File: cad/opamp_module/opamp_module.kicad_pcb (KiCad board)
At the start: 2 copper layers, 46.5 x 35.5 mm, 28 parts, among them J1 Conn_02x04_Odd_Even, U1 OPA2325, U2 REF3433IDBVR

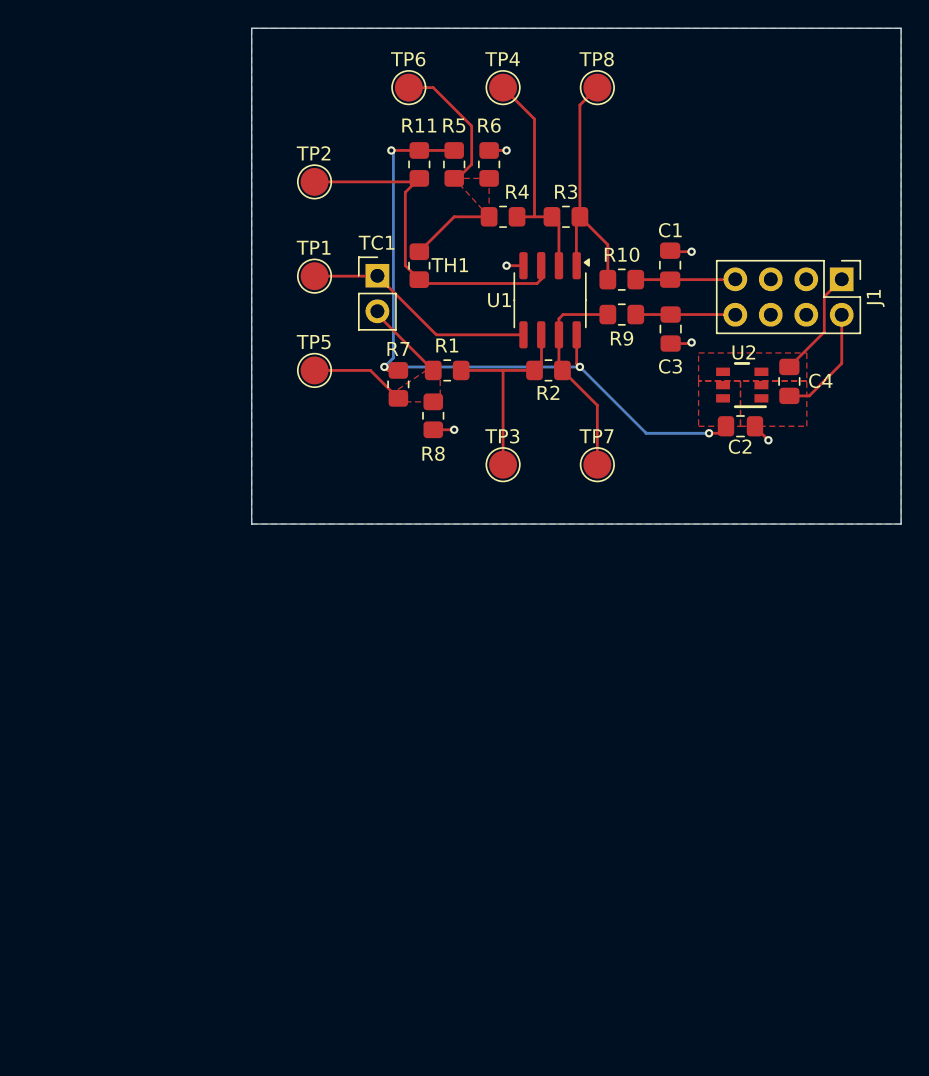
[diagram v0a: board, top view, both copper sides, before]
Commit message: Spice simulations and switching to two TC's per module
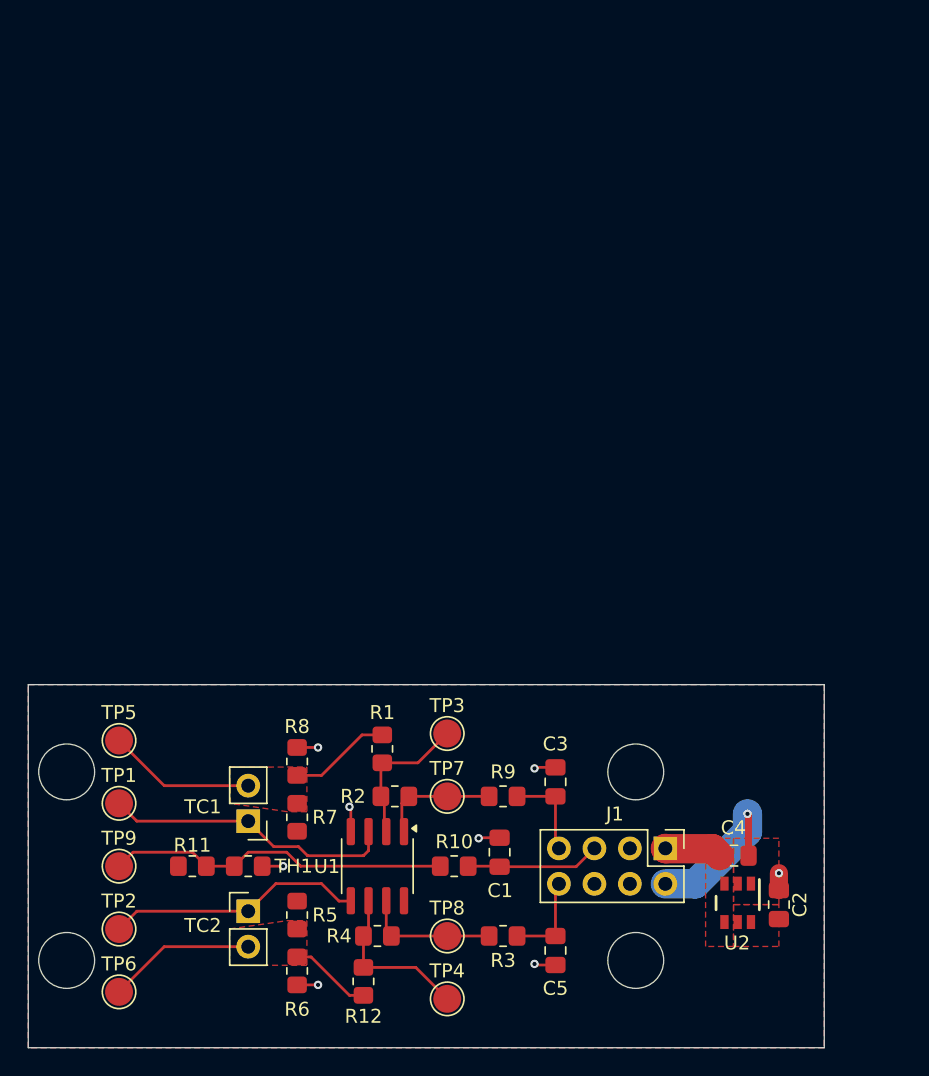
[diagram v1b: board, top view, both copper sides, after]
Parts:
- added C5: 47n, Capacitor_SMD:C_0805_2012Metric_Pad1.18x1.45mm_HandSolder, F.Cu at (143.8, 140.0)
- added R12: 10k, Resistor_SMD:R_0805_2012Metric_Pad1.20x1.40mm_HandSolder, F.Cu at (130.0, 142.2)
- added TC2: Thermocouple, Connector_PinHeader_2.54mm:PinHeader_1x02_P2.54mm_Vertical, F.Cu at (121.8, 137.2)
- added TP9: TestPoint, TestPoint:TestPoint_Pad_D2.0mm, F.Cu at (112.5, 134.0)
- R1: value 1M -> 10k
- R10, R9: value 1.7k -> 3386
- R11: value 3M3 -> 10k
- R2: value 32M -> 340k
- R3: value 12M -> 3386
- R4: value 1M -> 340k
- R5, R7: value 9000 -> 90k
- R6: value 2000 -> 500
- R8: value 4000 -> 500
- moved TP6 68.0 mm to (112.5, 143.0)
- moved TP4 65.4 mm to (136.0, 143.5)
- moved TP8 61.7 mm to (136.0, 139.0)
- moved R6 59.4 mm to (125.2, 141.5), turned to -90 degrees
- moved TP2 55.3 mm to (112.5, 138.5)
- moved R5 54.9 mm to (125.2, 137.5)
- moved R11 52.8 mm to (117.8, 134.0), turned to 180 degrees
- moved R4 52.3 mm to (131.0, 139.0)
- moved R3 51.7 mm to (140.0, 139.0), turned to 0 degrees
- moved TH1 44.7 mm to (121.8, 134.0), turned to 180 degrees
- moved C1 43.8 mm to (139.8, 133.0)
- moved R10 43.7 mm to (136.5, 134.0)
- moved J1 42.7 mm to (151.6, 132.7)
- moved U1 42.4 mm to (131.0, 134.0)
- moved TP1 40.3 mm to (112.5, 129.5)
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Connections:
- C3 pad 1: ThemoCoupleFiltered -> ThermoCoupleFiltered_{0}
- J1 pad 5: unconnected-(J1-Pin_5-Pad5) -> ThermistorFiltered
- J1 pad 7: ThermistorFiltered -> ThermoCoupleFiltered_{0}
- J1 pad 8: ThemoCoupleFiltered -> ThermoCoupleFiltered_{1}
- R1 pad 1: Net-(U1B--) -> OffsetReferenceThermoCouple_{0}
- R1 pad 2: OffsetReferenceThermoCouple -> Net-(U1A--)
- R11 pad 1: Net-(U1A-+) -> ThermistorUnfiltered
- R2 pad 1: ThemoCoupleUnfiltered -> ThermoCoupleUnfiltered_{0}
- R2 pad 2: Net-(U1B--) -> Net-(U1A--)
- R3 pad 1: ThermistorUnfiltered -> ThermoCoupleUnfiltered_{1}
- R3 pad 2: Net-(U1A--) -> ThermoCoupleFiltered_{1}
- R4 pad 1: Net-(U1A--) -> ThermoCoupleUnfiltered_{1}
- R4 pad 2: OffsetReferenceThermistor -> Net-(U1B--)
- R5 pad 2: OffsetReferenceThermistor -> OffsetReferenceThermoCouple_{1}
- R6 pad 1: OffsetReferenceThermistor -> OffsetReferenceThermoCouple_{1}
- R7 pad 2: OffsetReferenceThermoCouple -> OffsetReferenceThermoCouple_{0}
- R8 pad 1: OffsetReferenceThermoCouple -> OffsetReferenceThermoCouple_{0}
- R9 pad 1: ThemoCoupleUnfiltered -> ThermoCoupleUnfiltered_{0}
- R9 pad 2: ThemoCoupleFiltered -> ThermoCoupleFiltered_{0}
- TC1 pad 2: OffsetReferenceThermoCouple -> OffsetReferenceThermoCouple_{0}
- TH1 pad 1: OffsetReferenceThermistor -> GND
- TH1 pad 2: Net-(U1A-+) -> ThermistorUnfiltered
- TP2 pad 1: Net-(U1A-+) -> Net-(TC2-+)
- TP3 pad 1: Net-(U1B--) -> Net-(U1A--)
- TP4 pad 1: Net-(U1A--) -> Net-(U1B--)
- TP5 pad 1: OffsetReferenceThermoCouple -> OffsetReferenceThermoCouple_{0}
- TP6 pad 1: OffsetReferenceThermistor -> OffsetReferenceThermoCouple_{1}
- TP7 pad 1: ThemoCoupleUnfiltered -> ThermoCoupleUnfiltered_{0}
- TP8 pad 1: ThermistorUnfiltered -> ThermoCoupleUnfiltered_{1}
- U1 pad 1: ThermistorUnfiltered -> ThermoCoupleUnfiltered_{0}
- U1 pad 3: Net-(U1A-+) -> Net-(TC1-+)
- U1 pad 5: Net-(TC1-+) -> Net-(TC2-+)
- U1 pad 7: ThemoCoupleUnfiltered -> ThermoCoupleUnfiltered_{1}
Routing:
- net +3.3VA: track 50.5 -> 0.00 mm, vias 4 -> 0
- net Net-(U1A-+): track 25.6 -> 0.00 mm
- net Net-(TC2-+): track 0.00 -> 18.5 mm
- net OffsetReferenceThermoCouple_{0}: track 0.00 -> 17.9 mm
- net OffsetReferenceThermoCouple_{1}: track 0.00 -> 16.5 mm
- net OffsetReferenceThermistor: track 15.8 -> 0.00 mm
- net ThemoCoupleUnfiltered: track 15.2 -> 0.00 mm
- net OffsetReferenceThermoCouple: track 12.7 -> 0.00 mm
- net ThermoCoupleUnfiltered_{1}: track 0.00 -> 9.68 mm
- net ThermoCoupleUnfiltered_{0}: track 0.00 -> 8.55 mm
- net GND: track 16.7 -> 23.8 mm, vias 6 -> 9
- net ThemoCoupleFiltered: track 7.14 -> 0.00 mm
- net ThermoCoupleFiltered_{0}: track 0.00 -> 7.06 mm
- net ThermoCoupleFiltered_{1}: track 0.00 -> 6.10 mm
- net ThermistorUnfiltered: track 18.7 -> 24.7 mm
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- added copper zone on F.Cu, net OffsetReferenceThermoCouple_{0}
- added copper zone on F.Cu, net OffsetReferenceThermoCouple_{1}
- removed copper zone on F.Cu, net OffsetReferenceThermistor
- removed copper zone on F.Cu, net OffsetReferenceThermoCouple
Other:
- board size 46.5 x 35.5 mm -> 57 x 26 mm

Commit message: Ordered
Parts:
- R10, R3, R9: value 3386 -> 3.4k
- R5, R7: value 90k -> 90.9k
- R6, R8: value 500 -> 499
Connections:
- R1 pad 1: OffsetReferenceThermoCouple_{0} -> GND
- R12 pad 1: OffsetReferenceThermoCouple_{1} -> GND
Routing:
- net GND: track 23.8 -> 32.4 mm
- net OffsetReferenceThermoCouple_{0}: track 17.9 -> 10.6 mm
- net OffsetReferenceThermoCouple_{1}: track 16.5 -> 10.6 mm
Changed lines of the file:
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@@
 		(tags "Through hole pin header THT 1x02 2.54mm single row")
 		(property "Reference" "TC1"
-			(at 3.25 1.025 360)
+			(at 3.25 1.025 0)
 			(layer "F.SilkS")
 			(effects
@@
 		)
 		(property "Value" "Thermocouple"
-			(at 0 4.87 360)
+			(at 0 4.87 0)
 			(layer "F.Fab")
 			(effects
@@
 		(tags "capacitor handsolder")
 		(property "Reference" "C3"
-			(at 2.7125 0 360)
+			(at 2.7125 0 0)
 			(layer "F.SilkS")
 			(effects
@@
 		(tags "resistor handsolder")
 		(property "Reference" "R7"
-			(at 0 2 360)
+			(at 0 2 0)
 			(layer "F.SilkS")
 			(effects
@@
 			)
 		)
-		(property "Value" "90k"
+		(property "Value" "90.9k"
 			(at 0 1.65 90)
 			(layer "F.Fab")
@@
 		)
 		(property "Value" "Thermistor"
-			(at 0 1.65 360)
+			(at 0 1.65 0)
 			(layer "F.Fab")
 			(effects
@@
 		)
 		(fp_text user "${REFERENCE}"
-			(at 0 0 360)
+			(at 0 0 0)
 			(layer "F.Fab")
 			(effects
@@
 			)
 		)
-		(property "Value" "500"
+		(property "Value" "499"
 			(at 0 1.65 90)
 			(layer "F.Fab")
@@
 		(tags "resistor handsolder")
 		(property "Reference" "R4"
-			(at 2.75 0 360)
+			(at 2.75 0 0)
 			(layer "F.SilkS")
 			(effects
@@
 		)
 		(property "Value" "340k"
-			(at 0 1.65 360)
+			(at 0 1.65 0)
 			(layer "F.Fab")
 			(effects
@@
 		)
 		(fp_text user "${REFERENCE}"
-			(at 0 0 360)
+			(at 0 0 0)
 			(layer "F.Fab")
 			(effects
@@
 		(fp_arc
 			(start -0.576537 -0.906071)
-			(mid -0.449562 -1.033046)
+			(mid -0.449563 -1.033046)
 			(end -0.322588 -0.906071)
 			(stroke
@@
 		)
 		(property "Value" "1u"
-			(at 0 1.68 360)
+			(at 0 1.68 0)
 			(layer "F.Fab")
 			(effects
@@
 		)
 		(fp_text user "${REFERENCE}"
-			(at 0 0 360)
+			(at 0 0 0)
 			(layer "F.Fab")
 			(effects
@@
 			)
 		)
-		(property "Value" "3386"
+		(property "Value" "3.4k"
 			(at 0 1.65 0)
 			(layer "F.Fab")
@@
 			)
 		)
-		(property "Value" "3386"
+		(property "Value" "3.4k"
 			(at 0 1.65 0)
 			(layer "F.Fab")
@@
 			(layers "F.Cu" "F.Paste" "F.Mask")
 			(roundrect_rratio 0.208333)
-			(net 9 "OffsetReferenceThermoCouple_{0}")
+			(net 2 "GND")
 			(pintype "passive")
 		)
@@
 		(tags "resistor handsolder")
 		(property "Reference" "R6"
-			(at 2.75 0 360)
+			(at 2.75 0 0)
 			(layer "F.SilkS")
 			(effects
@@
 			)
 		)
-		(property "Value" "500"
+		(property "Value" "499"
 			(at 0 1.65 90)
 			(layer "F.Fab")
@@
 		(tags "resistor handsolder")
 		(property "Reference" "R3"
-			(at 0 1.75 360)
+			(at 0 1.75 0)
 			(layer "F.SilkS")
 			(effects
@@
 			)
 		)
-		(property "Value" "3386"
-			(at 0 1.65 360)
+		(property "Value" "3.4k"
+			(at 0 1.65 0)
 			(layer "F.Fab")
 			(effects
@@
 		)
 		(fp_text user "${REFERENCE}"
-			(at 0 0 360)
+			(at 0 0 0)
 			(layer "F.Fab")
 			(effects
@@
 		)
 		(property "Value" "10k"
-			(at 0 1.65 360)
+			(at 0 1.65 0)
 			(layer "F.Fab")
 			(effects
@@
 		)
 		(fp_text user "${REFERENCE}"
-			(at 0 0 360)
+			(at 0 0 0)
 			(layer "F.Fab")
 			(effects
@@
 			(layers "F.Cu" "F.Paste" "F.Mask")
 			(roundrect_rratio 0.208333)
-			(net 15 "OffsetReferenceThermoCouple_{1}")
+			(net 2 "GND")
 			(pintype "passive")
 		)
@@
 			)
 		)
-		(property "Value" "90k"
+		(property "Value" "90.9k"
 			(at 0 1.65 90)
 			(layer "F.Fab")
@@
 		(tags "resistor handsolder")
 		(property "Reference" "R2"
-			(at 3 0 360)
+			(at 3 0 0)
 			(layer "F.SilkS")
 			(effects
@@
 		)
 		(property "Value" "340k"
-			(at 0 1.65 360)
+			(at 0 1.65 0)
 			(layer "F.Fab")
 			(effects
@@
 		)
 		(fp_text user "${REFERENCE}"
-			(at 0 0 360)
+			(at 0 0 0)
 			(layer "F.Fab")
 			(effects
@@
 	)
 	(segment
+		(start 130 143.25)
+		(end 128.25 143.25)
+		(width 0.2)
+		(layer "F.Cu")
+		(net 2)
+	)
+	(segment
 		(start 125.25 142.5)
 		(end 126.75 142.5)
@@
 	)
 	(segment
+		(start 127.5 125.5)
+		(end 128.4 124.6)
+		(width 0.2)
+		(layer "F.Cu")
+		(net 2)
+	)
+	(segment
 		(start 124.25 134)
 		(end 122.75 134)
@@
 	)
 	(segment
+		(start 128.4 124.6)
+		(end 131.35 124.6)
+		(width 0.2)
+		(layer "F.Cu")
+		(net 2)
+	)
+	(segment
+		(start 126.75 125.5)
+		(end 127.5 125.5)
+		(width 0.2)
+		(layer "F.Cu")
+		(net 2)
+	)
+	(segment
 		(start 142.325 141.075)
 		(end 142.25 141)
@@
 	)
 	(segment
+		(start 127.5 142.5)
+		(end 126.75 142.5)
+		(width 0.2)
+		(layer "F.Cu")
+		(net 2)
+	)
+	(segment
+		(start 128.25 143.25)
+		(end 127.5 142.5)
+		(width 0.2)
+		(layer "F.Cu")
+		(net 2)
+	)
+	(segment
 		(start 159.75 135.7125)
 		(end 159.75 134.5)
@@
 	)
 	(segment
-		(start 129.9 124.6)
-		(end 131.35 124.6)
-		(width 0.2)
-		(layer "F.Cu")
-		(net 9)
-	)
-	(segment
-		(start 125.25 127.5)
-		(end 127 127.5)
-		(width 0.2)
-		(layer "F.Cu")
-		(net 9)
-	)
-	(segment
 		(start 115.735 128.235)
 		(end 112.5 125)
@@
 	)
 	(segment
-		(start 127 127.5)
-		(end 129.9 124.6)
-		(width 0.2)
-		(layer "F.Cu")
-		(net 9)
-	)
-	(segment
 		(start 130 141.25)
 		(end 133.75 141.25)
@@
 	)
 	(segment
-		(start 125.25 140.5)
-		(end 126.25 140.5)
-		(width 0.2)
-		(layer "F.Cu")
-		(net 15)
-	)
-	(segment
-		(start 129 143.25)
-		(end 130 143.25)
-		(width 0.2)
-		(layer "F.Cu")
-		(net 15)
-	)
-	(segment
-		(start 126.25 140.5)
-		(end 129 143.25)
-		(width 0.2)
-		(layer "F.Cu")
-		(net 15)
-	)
-	(segment
 		(start 121.75 139.765)
 		(end 115.735 139.765)
@@
 	)
 	(segment
-		(start 123.725 135.25)
-		(end 127 135.25)
+		(start 127 136.5)
+		(end 129.07 136.5)
 		(width 0.2)
 		(layer "F.Cu")
@@
 	)
 	(segment
-		(start 128.25 136.5)
-		(end 129.07 136.5)
+		(start 129.07 136.5)
+		(end 129.095 136.475)
 		(width 0.2)
 		(layer "F.Cu")
@@
 	)
 	(segment
-		(start 121.75 137.225)
-		(end 123.725 135.25)
+		(start 122.775 137.225)
+		(end 124.75 135.25)
 		(width 0.2)
 		(layer "F.Cu")
@@
 	)
 	(segment
-		(start 129.07 136.5)
-		(end 129.095 136.475)
+		(start 113.775 137.225)
+		(end 112.5 138.5)
 		(width 0.2)
 		(layer "F.Cu")
@@
 	)
 	(segment
-		(start 113.775 137.225)
-		(end 112.5 138.5)
+		(start 124.75 135.25)
+		(end 125.75 135.25)
 		(width 0.2)
 		(layer "F.Cu")
@@
 	)
 	(segment
-		(start 127 135.25)
-		(end 128.25 136.5)
+		(start 121.75 137.225)
+		(end 122.775 137.225)
+		(width 0.2)
+		(layer "F.Cu")
+		(net 18)
+	)
+	(segment
+		(start 125.75 135.25)
+		(end 127 136.5)
 		(width 0.2)
 		(layer "F.Cu")
@@
 		(polygon
 			(pts
-				(xy 124.55 137.9) (xy 125.95 137.9) (xy 125.95 141.1) (xy 120.42 141.095) (xy 120.42 138.495) (xy 120.42 138.495)
+				(xy 124.55 137.9) (xy 125.95 137.9) (xy 125.95 141.1) (xy 120.42 141.095) (xy 120.42 138.495)
 			)
 		)
